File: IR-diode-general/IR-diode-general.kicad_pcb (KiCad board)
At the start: 2 copper layers, 72.4 x 20.9 mm, 29 parts, among them J1 PJ-102A, J2 USB4105-GF-A, U1 MP2483DQ-LF-P, U2 AZ1117CH-5.0TRG1

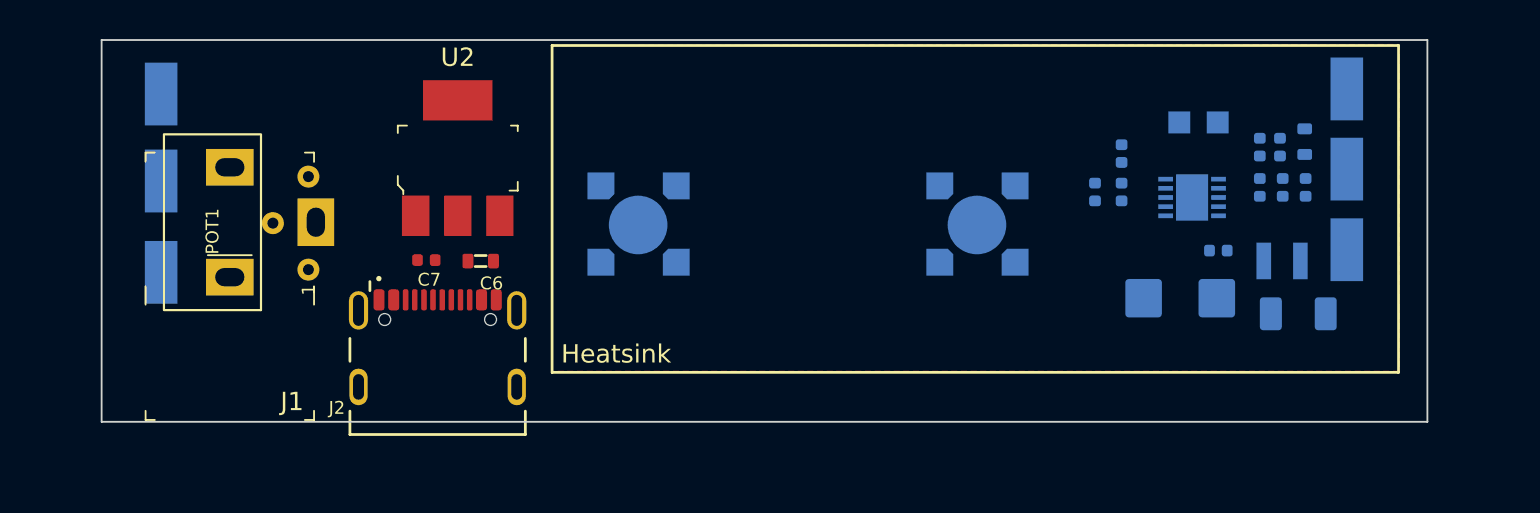
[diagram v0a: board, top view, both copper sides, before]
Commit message: Add preliminary layout
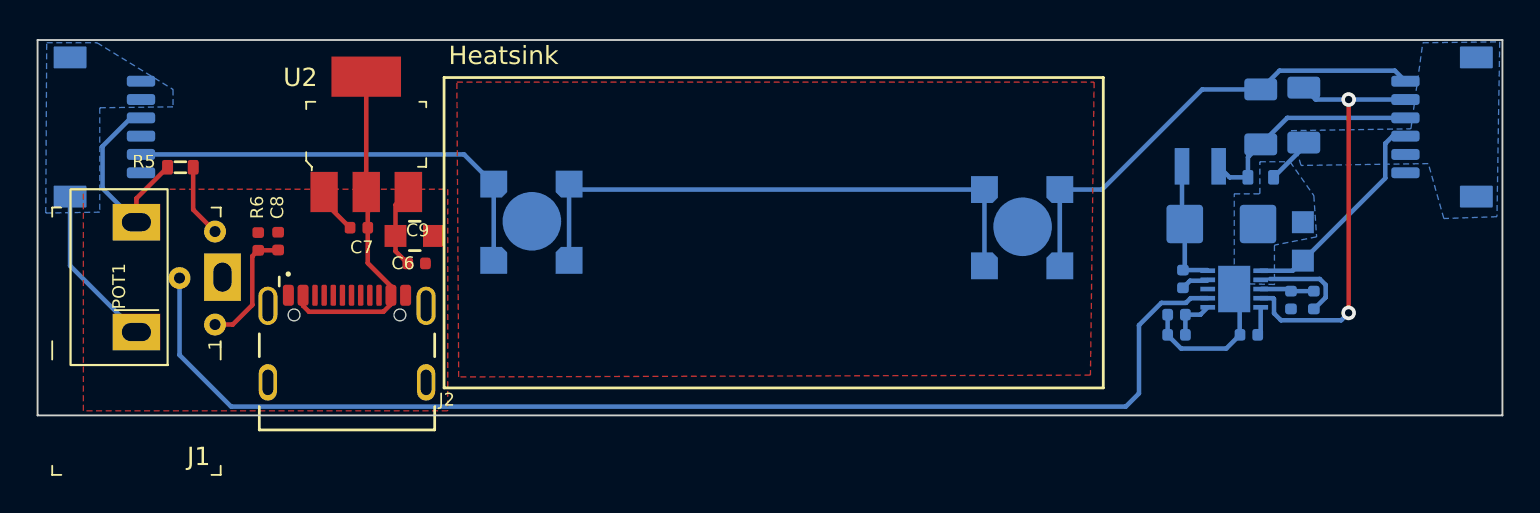
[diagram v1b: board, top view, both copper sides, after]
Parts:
- removed TP1, TP2, TP3, TP4, TP5, TP6: 5017, antmicro-footprints:PC_TEST-POINT_MINI_3.43x1.78mm
- added C9: C_100n_0402, antmicro-footprints:C_0402_1005Metric, F.Cu at (105.7, 52.7)
- added J3: SM06B-SRSS-TB-LF-SN, antmicro-footprints:JST_SM06B-SRSS-TB-LF-SN, B.Cu at (161.7, 45.3)
- added J4: SM06B-SRSS-TB-LF-SN, antmicro-footprints:JST_SM06B-SRSS-TB-LF-SN, B.Cu at (88.7, 45.2)
- added R7: R_0R_1206, antmicro-footprints:R_1206_3216Metric, B.Cu at (151.8, 44.7)
- C2: value C_2u2_0402 -> C_2u2_0603; footprint antmicro-footprints:C_0402_1005Metric -> antmicro-footprints:0603-cap
- C6: value C_10u_16V_0603 -> C_10u_0805; footprint antmicro-footprints:0603-cap -> antmicro-footprints:0805-cap
- C8, R5: moved to F.Cu
- R2: value R_100k_0.1%_0402 -> R_100k_0402; footprint antmicro-footprints:0402-res -> antmicro-footprints:R_0402_1005Metric
- R6: value R_20k_0.1%_0402 -> R_20k_0402; footprint antmicro-footprints:0402-res -> antmicro-footprints:R_0402_1005Metric; moved to F.Cu
- moved R5 61.4 mm to (92.8, 47.5), turned to 180 degrees
- moved R6 56.0 mm to (97.0, 51.5), turned to -90 degrees
- moved C8 53.9 mm to (98.1, 51.5), turned to -90 degrees
- moved D3 24.4 mm to (111.9, 50.5), turned to 0 degrees
- moved D2 20.9 mm to (138.7, 50.8), turned to 0 degrees
- moved R1 10.9 mm to (154.2, 44.6), turned to 90 degrees
- moved R2 8.98 mm to (147.2, 56.6), turned to 0 degrees
- moved C1 8.64 mm to (154.1, 51.5), turned to -90 degrees
- moved C3 7.62 mm to (147.6, 53.5)
- moved C5 7.34 mm to (147.2, 55.5), turned to 0 degrees
- moved L1 6.83 mm to (148.8, 47.4)
- moved R4 6.82 mm to (154.7, 54.7), turned to -90 degrees
- moved R3 6.17 mm to (153.4, 54.7), turned to 90 degrees
- moved J1 5.92 mm to (90.4, 53.4)
- moved POT1 5.92 mm to (89.5, 53.4)
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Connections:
- net Net-(C2-Pad2) renamed A_in
- net Net-(D2-Pad2) renamed C_in
- net Net-(D3-Pad1) renamed C_out
- C2 pad 1: Net-(C2-Pad1) -> GND
- D1 pad 1: (no net) -> GND
- D1 pad 2: (no net) -> Net-(C3-Pad1)
- U2 pad 2: unconnected-(U2-Pad2) -> Net-(C7-Pad2)
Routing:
- net Net-(POT1-Pad2): track 0.00 -> 66.2 mm
- net C_out: track 0.00 -> 47.5 mm, vias 0 -> 2
- net Net-(D2-Pad1): track 0.00 -> 31.1 mm
- net +12V: track 0.00 -> 28.5 mm
- net GND: track 0.00 -> 27.1 mm
- net C_in: track 0.00 -> 26.0 mm
- net Net-(C7-Pad2): track 0.00 -> 18.7 mm
- net A_in: track 0.00 -> 12.4 mm
- net Net-(C3-Pad1): track 0.00 -> 7.14 mm
- net Net-(C8-Pad2): track 0.00 -> 6.69 mm
- net Net-(POT1-Pad3): track 0.00 -> 4.00 mm
- net Net-(R3-Pad2): track 0.00 -> 3.07 mm
- net Net-(C5-Pad2): track 0.00 -> 2.49 mm
- net Net-(C4-Pad2): track 0.00 -> 1.57 mm
- net Net-(C3-Pad2): track 0.00 -> 1.53 mm
- added copper zone on B.Cu, net GND
- added copper zone on F.Cu, net GND
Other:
- board size 72.4 x 20.9 mm -> 80 x 20.5 mm
